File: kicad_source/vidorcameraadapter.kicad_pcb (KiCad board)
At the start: 2 copper layers, 62 x 63 mm, 70 parts, among them CN1 TE_2041119-2, CN2 RS2-20-G, CN3 DNI, U1 SN74LVC2G34DBV

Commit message: restored design files from master
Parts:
- R25, R26, R27, R28, R29: value 3k3 -> 1k
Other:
- outline, holes or cut-outs redrawn
- board text added: "VidorCameraAdapter 0.1"
- board text removed: "VidorCameraAdapter dev_0.2"

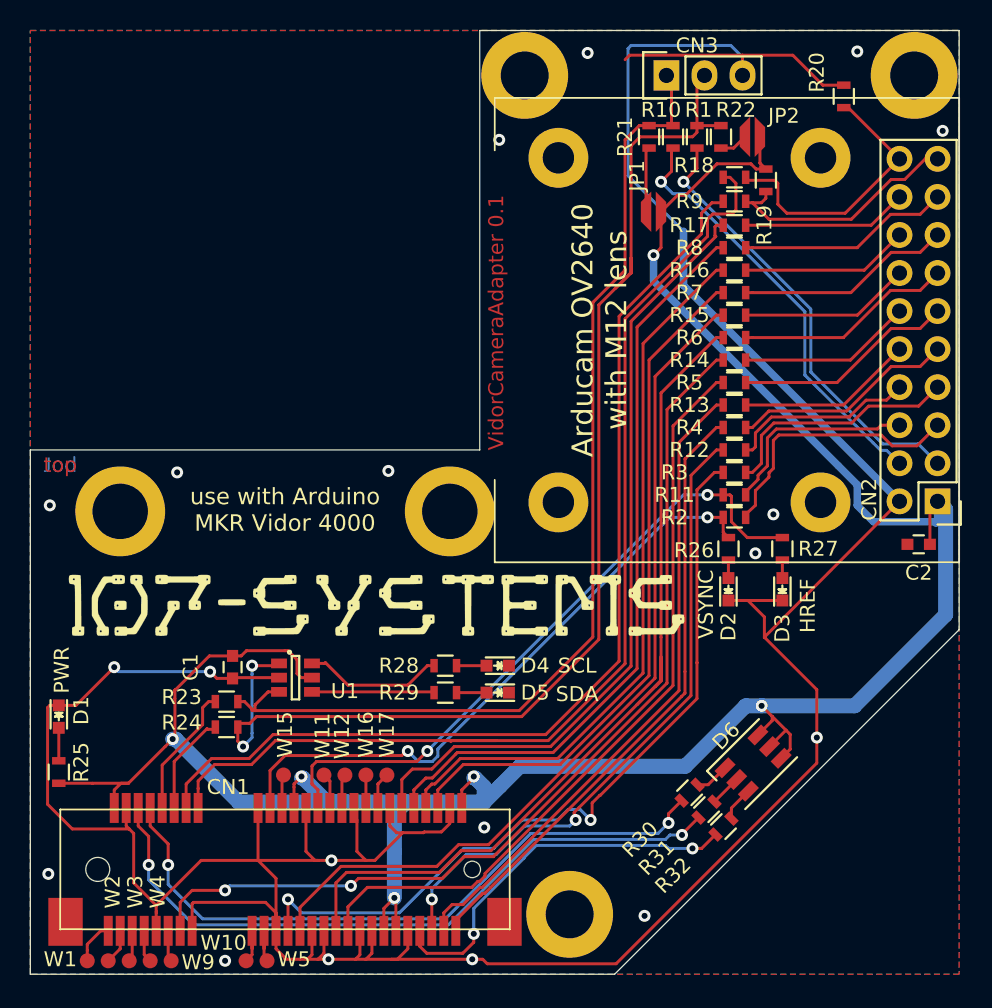
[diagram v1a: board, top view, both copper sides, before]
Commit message: made pcb smaller to avoid collision with MKR connector
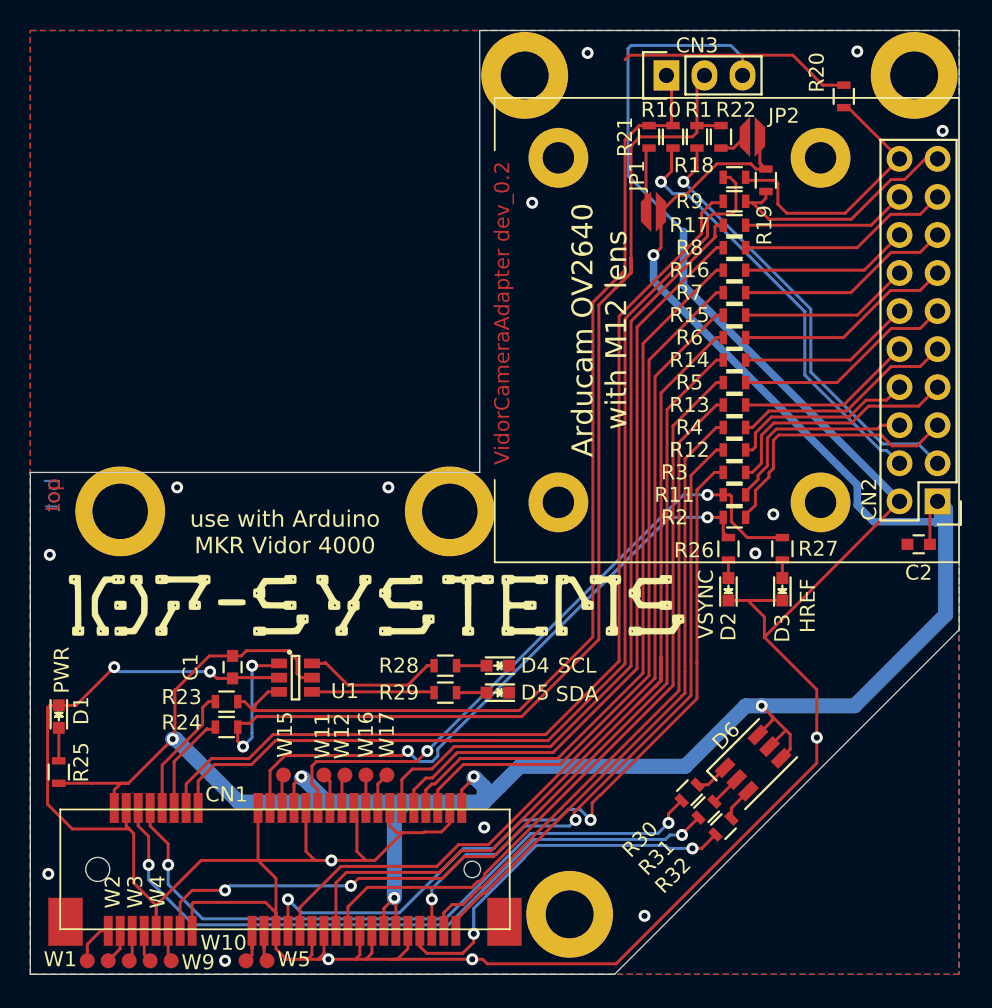
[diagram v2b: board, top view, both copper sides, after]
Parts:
- R25, R26, R27, R28, R29: value 1k -> 3k3
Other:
- outline, holes or cut-outs redrawn
- board text added: "VidorCameraAdapter dev_0.2"
- board text removed: "VidorCameraAdapter 0.1"
